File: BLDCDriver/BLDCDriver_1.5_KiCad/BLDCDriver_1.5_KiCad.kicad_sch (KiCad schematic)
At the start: 66 parts, among them IC1 STSPIN32G4, J2 Debug, J2 FFC_11P_1mm, J4 POWER, J5 CAN, SW1 SW_Push, U3 MCP2562-E-SN, U5 AS5048A-HTSP-500, U6 AP7375-50SA

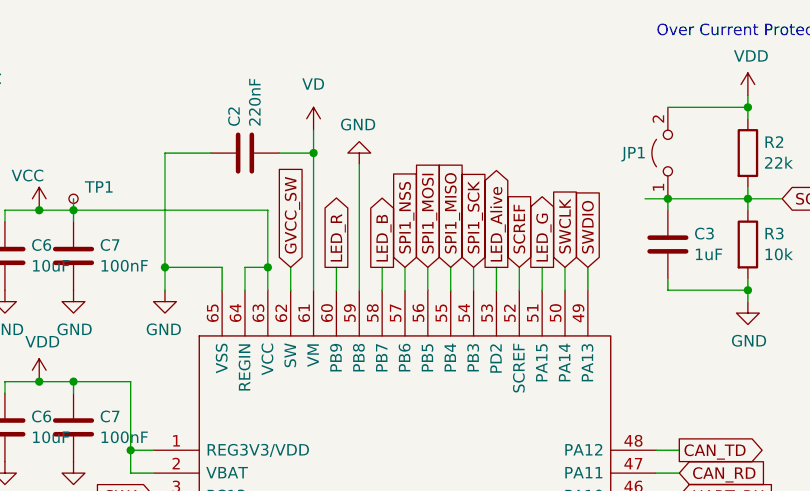
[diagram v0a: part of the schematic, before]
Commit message: ⚠️電源のシルク逆、SPI_CS繋がってないのを修正、GNDベタ最適化、Production
結構気づかなかったらやばかったやつばっかり
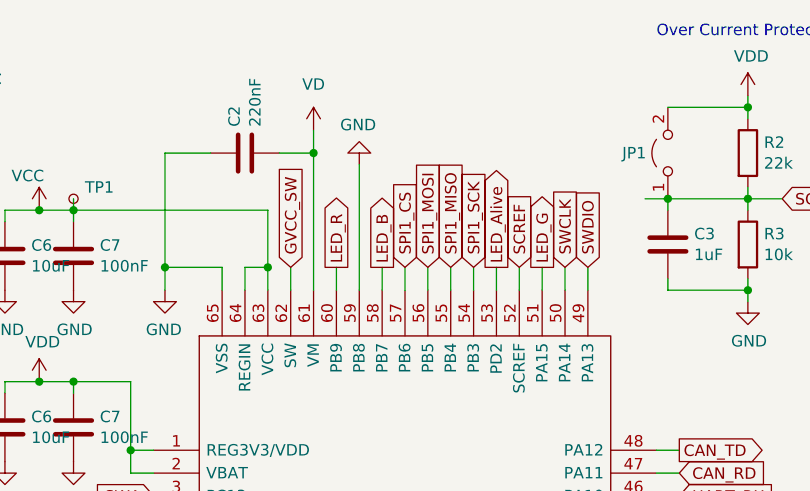
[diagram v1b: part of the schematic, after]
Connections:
- net SPI1_NSS is gone; now on net SPI1_CS: IC1.57 (PB6)
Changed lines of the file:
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@@
     )
   )
-  (global_label "SPI1_NSS" (shape input) (at 96.52 45.72 90) (fields_autoplaced)
+  (global_label "SPI1_CS" (shape input) (at 96.52 45.72 90) (fields_autoplaced)
     (effects (font (size 1.27 1.27)) (justify left))
-    (property "Intersheetrefs" "${INTERSHEET_REFS}" (at 96.52 34.1727 90)
+    (property "Intersheetrefs" "${INTERSHEET_REFS}" (at 96.52 35.2708 90)
       (effects (font (size 1.27 1.27)) (justify left) hide)
     )

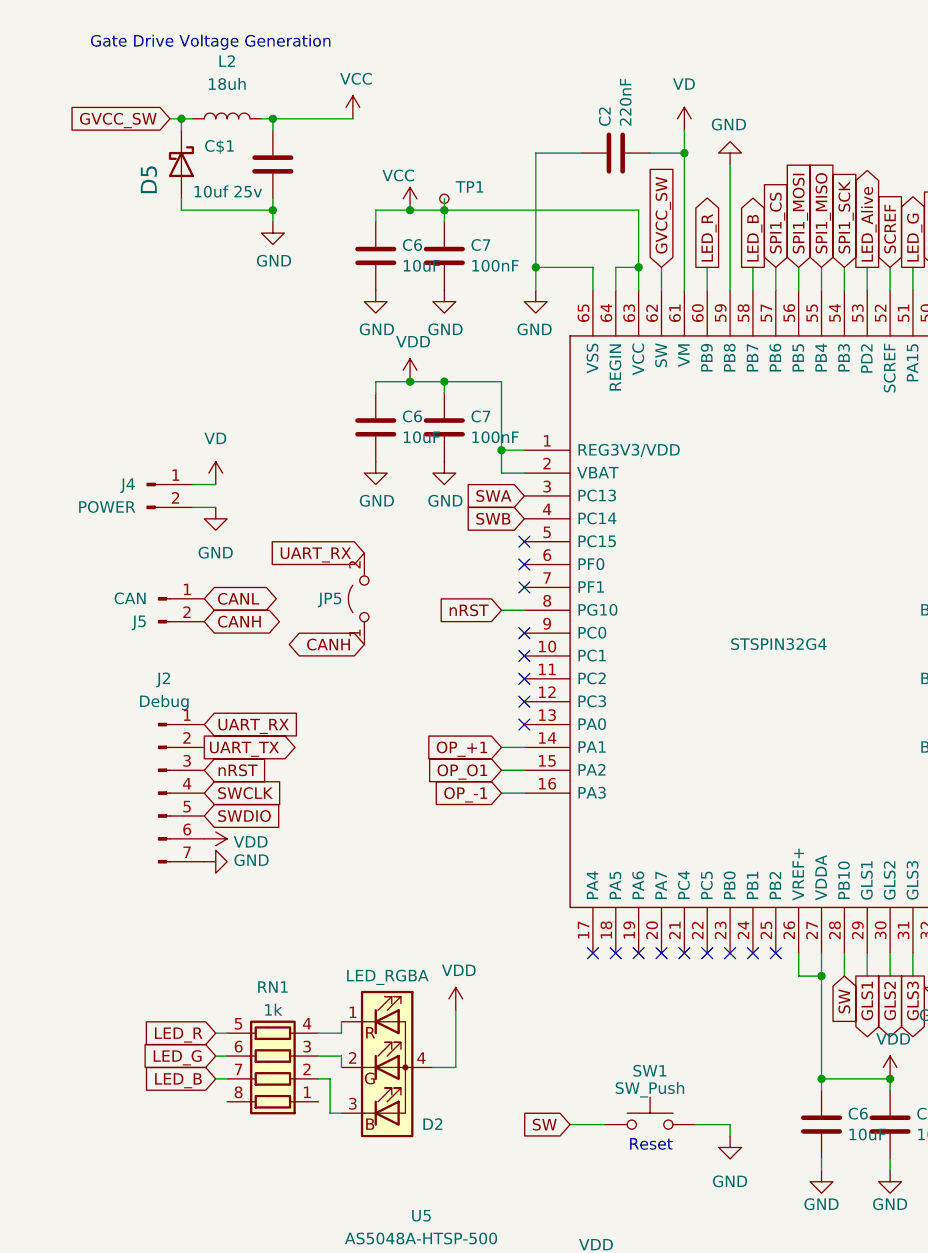
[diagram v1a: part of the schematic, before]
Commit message: ✏️LEDのRGBの配線を修正・Lチカを確認・DCDCの出力にコンデンサを追加
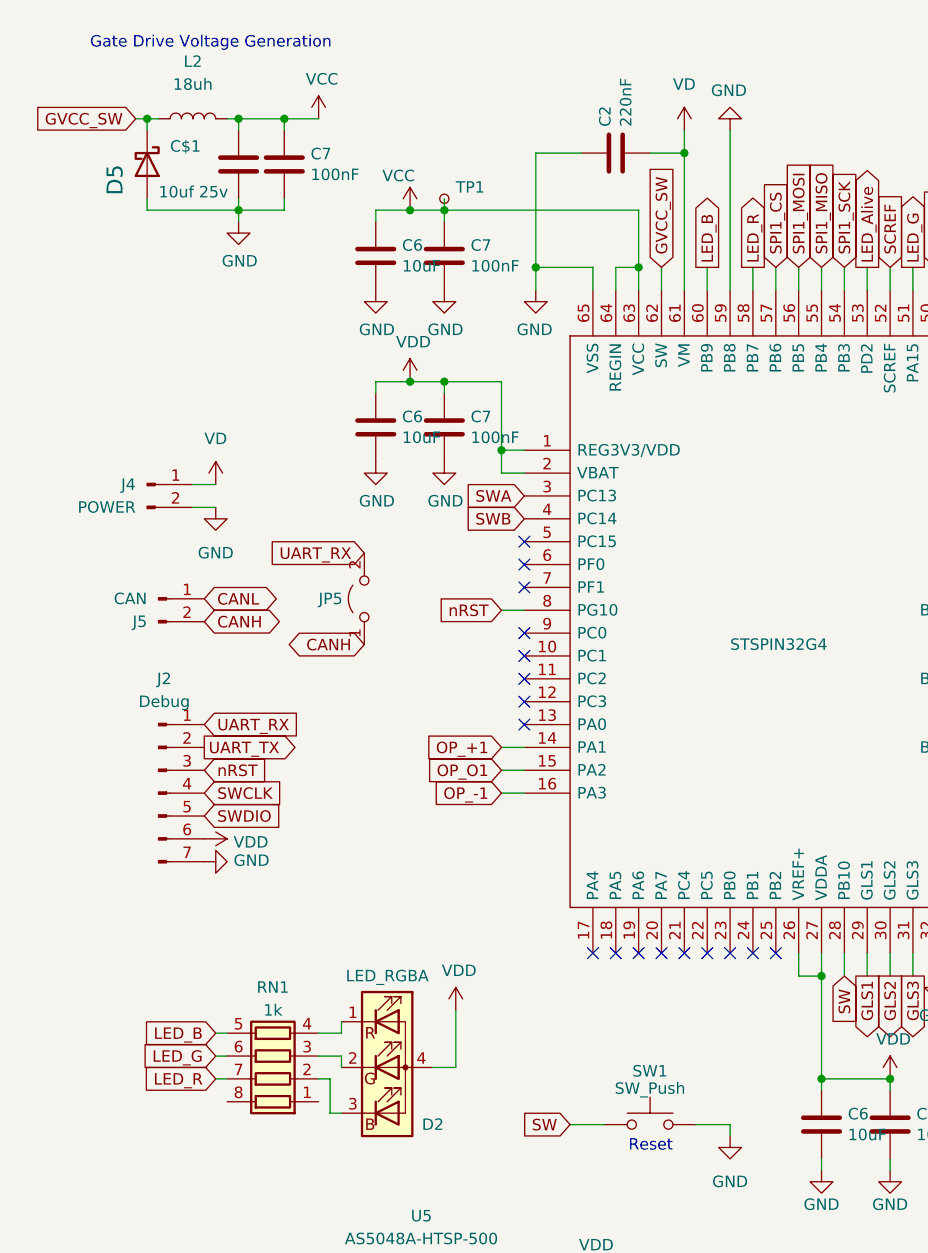
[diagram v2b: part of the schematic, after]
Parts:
- added C7: 100nF, Capacitor_SMD:C_0402_1005Metric, symbol Device:C
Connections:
- net GND: now also C7.2
- net LED_B: now also IC1.60 (PB9), RN1.5 (R4.2); no longer IC1.58 (PB7), RN1.7 (R2.2)
- net LED_R: now also IC1.58 (PB7), RN1.7 (R2.2); no longer IC1.60 (PB9), RN1.5 (R4.2)
- net VCC: now also C7.1
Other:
- moved on the sheet: C$1, D5, L2

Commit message: ✨フットプリントをMAX3051に変更
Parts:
- added C26: 100nF, Capacitor_SMD:C_0402_1005Metric, symbol Device:C
- added R20: 120, Resistor_SMD:R_0603_1608Metric_Pad0.98x0.95mm_HandSolder, symbol Device:R
- added U7: MAX3051ESA_, BLDC:SOIC127P600X175-8N, symbol BLDC_sym:MAX3051ESA_
- C7, R14, U3, U6: now not fitted
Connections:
- net CANH: now also R20.1, U7.7 (CANH)
- net CANL: now also R20.2, U7.6 (CANL)
- net CAN_RD: now also U7.4 (RXD)
- net CAN_TD: now also U7.1 (TXD)
- net GND: now also C26.2, U7.2 (GND), U7.8 (RS)
- net VDD: now also C26.1, U7.3 (VCC)
- no-connect marks 27 -> 28
